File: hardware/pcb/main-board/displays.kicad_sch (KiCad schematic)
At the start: 1 part, among them J601 DISP_PCB x40 FPC

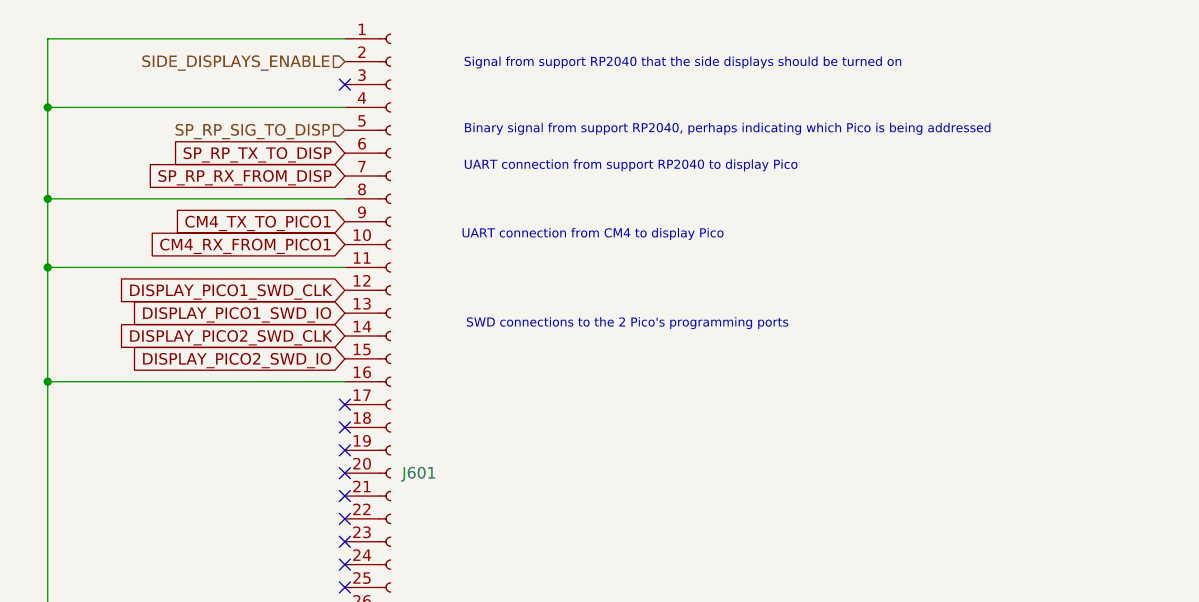
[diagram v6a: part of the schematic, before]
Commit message: update support pico links: UART0 to CM4, UART1 to app board Pico0, GPIOs to app board Pico1. KB pico outstanding
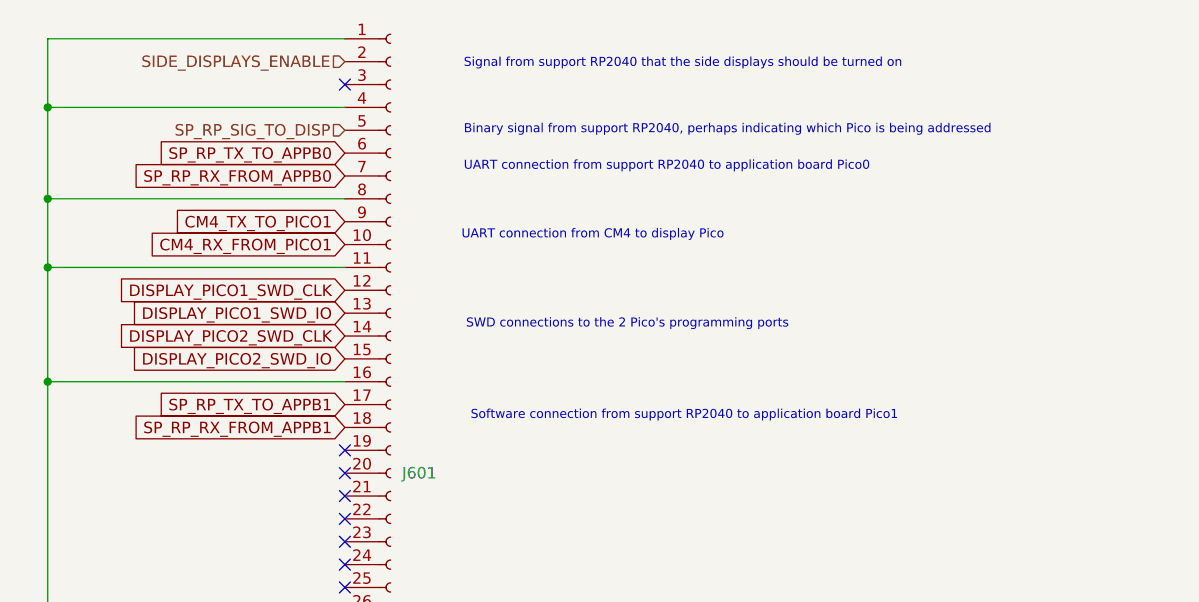
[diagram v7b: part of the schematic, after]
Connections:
- net SP_RP_TX_TO_APPB1: now reaches J601.17 (Pin_17)
- net SP_RP_RX_FROM_APPB1: now reaches J601.18 (Pin_18)
- net SP_RP_RX_FROM_DISP renamed SP_RP_RX_FROM_APPB0
- net SP_RP_TX_TO_DISP renamed SP_RP_TX_TO_APPB0
- no-connect marks 17 -> 15
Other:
- note added: "Software connection from support RP2040 to application board Pico1"
- note added: "UART connection from support RP2040 to application board Pico0"
- note removed: "UART connection from support RP2040 to display Pico"
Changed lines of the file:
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@@
-	)
-	(no_connect
-		(at 58.42 66.04)
 	)
 	(no_connect
@@
 	)
 	(no_connect
-		(at 58.42 63.5)
-	)
-	(no_connect
 		(at 58.42 73.66)
 	)
@@
 		)
 	)
-	(text "UART connection from support RP2040 to display Pico"
+	(text "Software connection from support RP2040 to application board Pico1"
+		(exclude_from_sim no)
+		(at 72.39 64.77 0)
+		(effects
+			(font
+				(size 1 1)
+			)
+			(justify left)
+		)
+	)
+	(text "UART connection from support RP2040 to application board Pico0"
 		(exclude_from_sim no)
 		(at 71.628 37.084 0)
@@
 		)
 	)
+	(global_label "SP_RP_RX_FROM_APPB1"
+		(shape input)
+		(at 58.42 66.04 180)
+		(fields_autoplaced yes)
+		(effects
+			(font
+				(size 1.27 1.27)
+			)
+			(justify right)
+		)
+		(property "Intersheetrefs" "${INTERSHEET_REFS}"
+			(at 33.471 66.04 0)
+			(effects
+				(font
+					(size 1.27 1.27)
+				)
+				(justify right)
+				(hide yes)
+			)
+		)
+	)
 	(global_label "DISPLAY_PICO2_SWD_CLK"
 		(shape input)
@@
 		)
 	)
-	(global_label "SP_RP_TX_TO_DISP"
+	(global_label "SP_RP_TX_TO_APPB0"
 		(shape input)
 		(at 58.42 35.56 180)
@@
 		)
 		(property "Intersheetrefs" "${INTERSHEET_REFS}"
-			(at 38.3696 35.56 0)
+			(at 36.6158 35.56 0)
 			(effects
 				(font
@@
 		)
 	)
-	(global_label "SP_RP_RX_FROM_DISP"
+	(global_label "SP_RP_TX_TO_APPB1"
+		(shape input)
+		(at 58.42 63.5 180)
+		(fields_autoplaced yes)
+		(effects
+			(font
+				(size 1.27 1.27)
+			)
+			(justify right)
+		)
+		(property "Intersheetrefs" "${INTERSHEET_REFS}"
+			(at 36.6158 63.5 0)
+			(effects
+				(font
+					(size 1.27 1.27)
+				)
+				(justify right)
+				(hide yes)
+			)
+		)
+	)
+	(global_label "SP_RP_RX_FROM_APPB0"
 		(shape input)
 		(at 58.42 38.1 180)
@@
 		)
 		(property "Intersheetrefs" "${INTERSHEET_REFS}"
-			(at 35.2248 38.1 0)
-			(effects
-				(font
+			(at 33.471 38.1 0)
+			(effects
+				(font

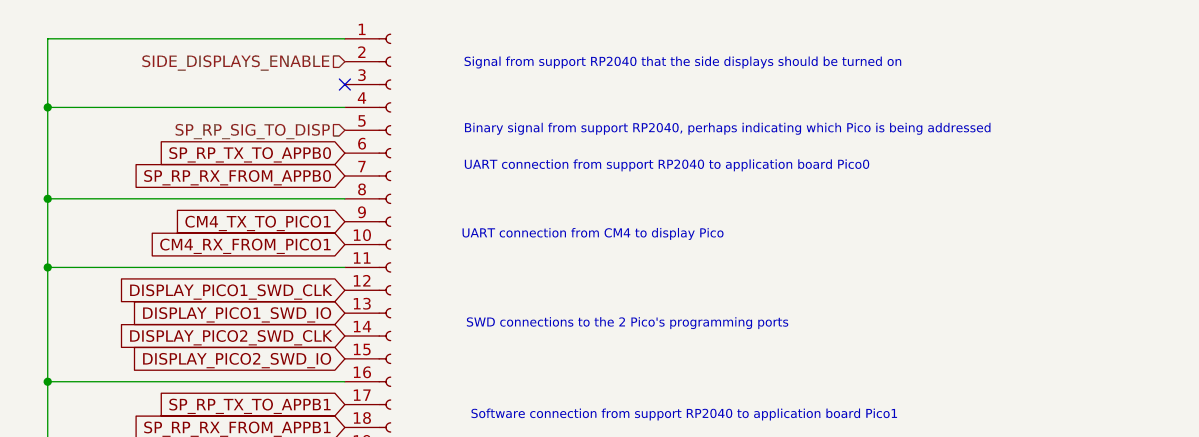
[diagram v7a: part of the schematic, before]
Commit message: rename display board things to application board things
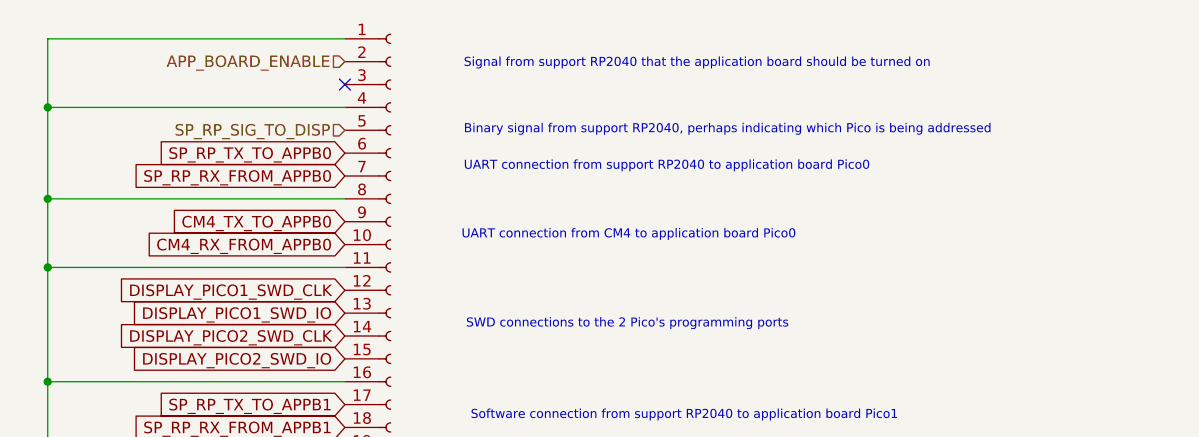
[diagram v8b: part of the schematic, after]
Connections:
- net CM4_RX_FROM_PICO1 renamed CM4_RX_FROM_APPB0
- net CM4_TX_TO_PICO1 renamed CM4_TX_TO_APPB0
- net SIDE_DISPLAYS_ENABLE renamed APP_BOARD_ENABLE
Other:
- note added: "Signal from support RP2040 that the application board should be turned on"
- note added: "UART connection from CM4 to application board Pico0"
- note removed: "Signal from support RP2040 that the side displays should be turned on"
- note removed: "UART connection from CM4 to display Pico"
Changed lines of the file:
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@@
 		)
 	)
-	(text "Signal from support RP2040 that the side displays should be turned on"
+	(text "Signal from support RP2040 that the application board should be turned on"
 		(exclude_from_sim no)
 		(at 71.628 25.654 0)
@@
 		)
 	)
-	(text "UART connection from CM4 to display Pico"
+	(text "UART connection from CM4 to application board Pico0"
 		(exclude_from_sim no)
 		(at 71.374 44.704 0)
@@
 		)
 	)
-	(global_label "CM4_RX_FROM_PICO1"
+	(global_label "CM4_RX_FROM_APPB0"
 		(shape input)
 		(at 58.42 45.72 180)
@@
 		)
 		(property "Intersheetrefs" "${INTERSHEET_REFS}"
-			(at 35.9505 45.72 0)
+			(at 35.5272 45.72 0)
 			(effects
 				(font
@@
 		)
 	)
-	(global_label "CM4_TX_TO_PICO1"
+	(global_label "CM4_TX_TO_APPB0"
 		(shape input)
 		(at 58.42 43.18 180)
@@
 		)
 		(property "Intersheetrefs" "${INTERSHEET_REFS}"
-			(at 39.0953 43.18 0)
+			(at 38.672 43.18 0)
 			(effects
 				(font
@@
 		)
 	)
-	(hierarchical_label "SIDE_DISPLAYS_ENABLE"
+	(hierarchical_label "APP_BOARD_ENABLE"
 		(shape input)
 		(at 58.42 25.4 180)
